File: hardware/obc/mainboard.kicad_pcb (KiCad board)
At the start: 6 copper layers, 95.9 x 90.2 mm, 216 parts, among them J101 Conn_02x20_Odd_Even, J301 USB_C_Receptacle_USB2.0, J302 Conn_High-Rel_4S2P, J303 Conn_01x06, J304 Conn_High-Rel_6P, J305 Conn_01x05, J601 Conn_01x08_Socket, J602 SMA RA Connector, J603 SMA RA Connector, J604 SMA RA Connector, Q201 BSS138DWQ-7, Q202 BSS138DWQ-7, Q203 MBT2222ADW1T1, Q204 MBT2222ADW1T1, Q205 BSS138DWQ-7, Q206 BSS138DWQ-7, Q207 MBT2222ADW1T1, Q208 MBT2222ADW1T1, Q209 MMDT2907, Q401 MBT2222ADW1T1, Q402 MBT2222ADW1T1, Q403 IRLML2803, Q404 IRF7406PbF, Q501 MMBT2222AT, Q502 IRLML2803, Q503 IRLML2803, Q504 IRLML2803, Q505 IRF7406PbF, Q506 IRF7406PbF, Q507 IRF7406PbF, U101 MAX706RESA, U102 ATSAMD51J20A-AU, U103 BMI088, U301 Mem_MT29F4G01ABAFDWB, U302 Mem_MT29F4G01ABAFDWB, U401 TPS7A4501DCQT, U402 LTC4121, U403 TPS54226PWPRPWP14_2P31X2P46-L, U404 ADM1176-1ARMZ-R7, U405 BQ25886RGER, U501 PE014006, U601 RFM98PW, U602 S1216V8, U603 GP2S1+, Y101 32.768kHz

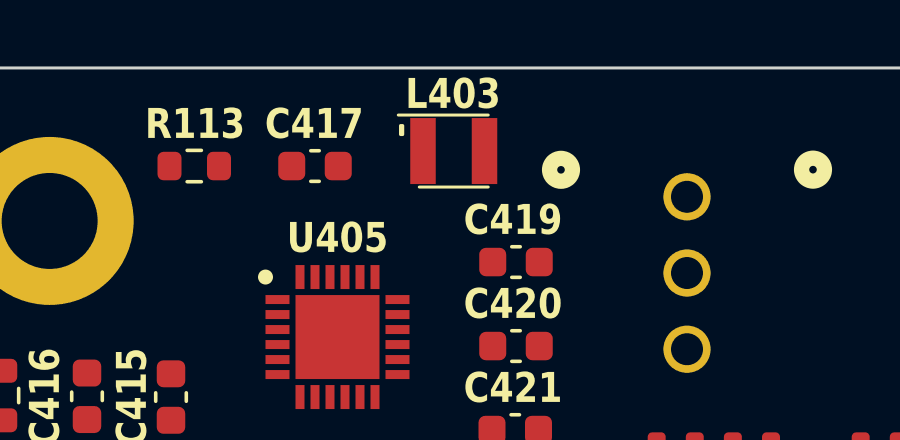
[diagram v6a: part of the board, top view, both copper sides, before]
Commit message: obc: various changes from design review
- change 1008 inductor footprint to one from kicad library
- change 'default class' design rules to match board design rules
- back-annotate from layout to board
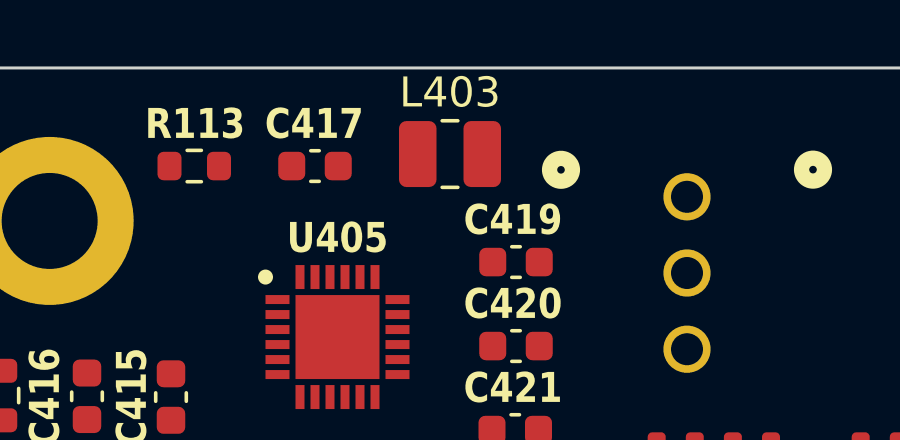
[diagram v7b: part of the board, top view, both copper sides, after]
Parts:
- L403: footprint SSE_Footprints:Murata_1008_2.5x2.0mm -> Inductor_SMD:L_1008_2520Metric
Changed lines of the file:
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@@
 		)
 	)
-	(footprint "SSE_Footprints:Murata_1008_2.5x2.0mm"
+	(footprint "Inductor_SMD:L_1008_2520Metric"
 		(layer "F.Cu")
 		(at 119.3 61.1)
+		(descr "Inductor SMD 1008 (2520 Metric), square (rectangular) end terminal, IPC_7351 nominal, (Body size source: https://ecsxtal.com/store/pdf/ECS-MPI2520-SMD-POWER-INDUCTOR.pdf), generated with kicad-footprint-generator")
+		(tags "inductor")
 		(property "Reference" "L403"
-			(at 0.1 -2 0)
-			(unlocked yes)
+			(at 0 -2.05 0)
 			(layer "F.SilkS")
 			(effects
 				(font
-					(size 1 0.85)
-					(thickness 0.13)
-					(bold yes)
+					(size 1 1)
+					(thickness 0.15)
 				)
 			)
 		)
 		(property "Value" "1uH"
-			(at 0 1.9 0)
-			(unlocked yes)
+			(at 0 2.05 0)
 			(layer "F.Fab")
 			(effects
@@
 			(effects
 				(font
-					(size 1 1)
-					(thickness 0.15)
+					(size 1.27 1.27)
 				)
 			)
@@
 			(effects
 				(font
-					(size 1 1)
-					(thickness 0.15)
+					(size 1.27 1.27)
 				)
 			)
@@
 			(effects
 				(font
-					(size 1 1)
-					(thickness 0.15)
+					(size 1.27 1.27)
 				)
 			)
@@
 			)
 		)
-		(property ki_fp_filters "Choke_* *Coil* Inductor_* L_*")
-		(sheetname "Power")
-		(sheetfile "Power.kicad_sch")
 		(attr smd)
 		(fp_line
-			(start -1.725 -1.3)
-			(end 1.275 -1.3)
-			(stroke
-				(width 0.1)
+			(start -0.261252 -1.11)
+			(end 0.261252 -1.11)
+			(stroke
+				(width 0.12)
 				(type solid)
 			)
@@
 		)
 		(fp_line
-			(start 1.275 1.1)
-			(end -1.025 1.1)
-			(stroke
-				(width 0.1)
+			(start -0.261252 1.11)
+			(end 0.261252 1.11)
+			(stroke
+				(width 0.12)
 				(type solid)
 			)
 			(layer "F.SilkS")
 		)
-		(fp_rect
-			(start -1.65 -0.95)
-			(end -1.575 -0.65)
-			(stroke
-				(width 0.1)
-				(type solid)
-			)
-			(fill solid)
-			(layer "F.SilkS")
-		)
-		(fp_line
-			(start -1.875 -1.4)
-			(end 2.125 -1.4)
-			(stroke
-				(width 0.05)
-				(type solid)
-			)
-			(layer "F.CrtYd")
-		)
-		(fp_line
-			(start -1.875 1.2)
-			(end -1.875 -1.4)
-			(stroke
-				(width 0.05)
-				(type solid)
-			)
-			(layer "F.CrtYd")
-		)
-		(fp_line
-			(start 2.125 -1.4)
-			(end 2.125 1.2)
-			(stroke
-				(width 0.05)
-				(type solid)
-			)
-			(layer "F.CrtYd")
-		)
-		(fp_line
-			(start 2.125 1.2)
-			(end -1.875 1.2)
-			(stroke
-				(width 0.05)
-				(type solid)
-			)
-			(layer "F.CrtYd")
-		)
-		(fp_line
-			(start -1.125 -1.1)
-			(end 1.375 -1.1)
-			(stroke
-				(width 0.1)
-				(type solid)
-			)
-			(layer "F.Fab")
-		)
-		(fp_line
-			(start -1.125 0.9)
-			(end -1.125 -1.1)
-			(stroke
-				(width 0.1)
-				(type solid)
-			)
-			(layer "F.Fab")
-		)
-		(fp_line
-			(start 1.375 -1.1)
-			(end 1.375 0.9)
-			(stroke
-				(width 0.1)
-				(type solid)
-			)
-			(layer "F.Fab")
-		)
-		(fp_line
-			(start 1.375 0.9)
-			(end -1.125 0.9)
+		(fp_line
+			(start -1.95 -1.35)
+			(end 1.95 -1.35)
+			(stroke
+				(width 0.05)
+				(type solid)
+			)
+			(layer "F.CrtYd")
+		)
+		(fp_line
+			(start -1.95 1.35)
+			(end -1.95 -1.35)
+			(stroke
+				(width 0.05)
+				(type solid)
+			)
+			(layer "F.CrtYd")
+		)
+		(fp_line
+			(start 1.95 -1.35)
+			(end 1.95 1.35)
+			(stroke
+				(width 0.05)
+				(type solid)
+			)
+			(layer "F.CrtYd")
+		)
+		(fp_line
+			(start 1.95 1.35)
+			(end -1.95 1.35)
+			(stroke
+				(width 0.05)
+				(type solid)
+			)
+			(layer "F.CrtYd")
+		)
+		(fp_line
+			(start -1.25 -1)
+			(end 1.25 -1)
+			(stroke
+				(width 0.1)
+				(type solid)
+			)
+			(layer "F.Fab")
+		)
+		(fp_line
+			(start -1.25 1)
+			(end -1.25 -1)
+			(stroke
+				(width 0.1)
+				(type solid)
+			)
+			(layer "F.Fab")
+		)
+		(fp_line
+			(start 1.25 -1)
+			(end 1.25 1)
+			(stroke
+				(width 0.1)
+				(type solid)
+			)
+			(layer "F.Fab")
+		)
+		(fp_line
+			(start 1.25 1)
+			(end -1.25 1)
 			(stroke
 				(width 0.1)
@@
 		)
 		(fp_text user "${REFERENCE}"
-			(at -0.1 -0.1 0)
-			(unlocked yes)
-			(layer "F.Fab")
-			(effects
-				(font
-					(size 1 1)
-					(thickness 0.15)
-				)
-			)
-		)
-		(pad "1" smd rect
-			(at -0.9 -0.1)
-			(size 0.85 2.2)
+			(at 0 0 0)
+			(layer "F.Fab")
+			(effects
+				(font
+					(size 0.62 0.62)
+					(thickness 0.09)
+				)
+			)
+		)
+		(pad "1" smd roundrect
+			(at -1.075 0)
+			(size 1.25 2.2)
 			(layers "F.Cu" "F.Paste" "F.Mask")
+			(roundrect_rratio 0.2)
 			(net 30 "Net-(U405-PMID_1)")
 			(pinfunction "1")
 			(pintype "passive")
 		)
-		(pad "2" smd rect
-			(at 1.15 -0.1)
-			(size 0.85 2.2)
+		(pad "2" smd roundrect
+			(at 1.075 0)
+			(size 1.25 2.2)
 			(layers "F.Cu" "F.Paste" "F.Mask")
+			(roundrect_rratio 0.2)
 			(net 31 "Net-(U405-SW_1)")
 			(pinfunction "2")
 			(pintype "passive")
 		)
+		(model "${KICAD8_3DMODEL_DIR}/Inductor_SMD.3dshapes/L_1008_2520Metric.wrl"
+			(offset
+				(xyz 0 0 0)
+			)
+			(scale
+				(xyz 1 1 1)
+			)
+			(rotate
+				(xyz 0 0 0)
+			)
+		)
 	)

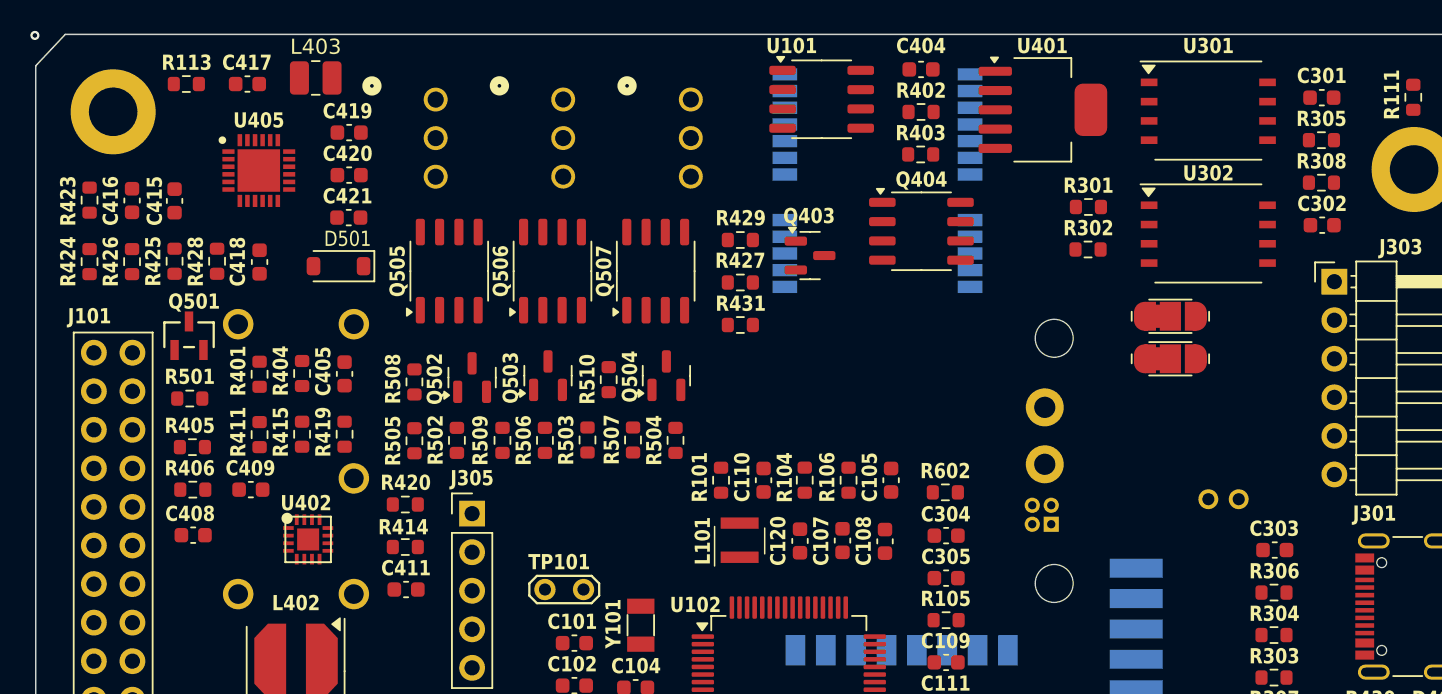
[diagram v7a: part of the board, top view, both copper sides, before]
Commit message: obc: entered footprint and routed traces in a test subsection
Made harwin battery connector vertical and routed traces around U405 component.
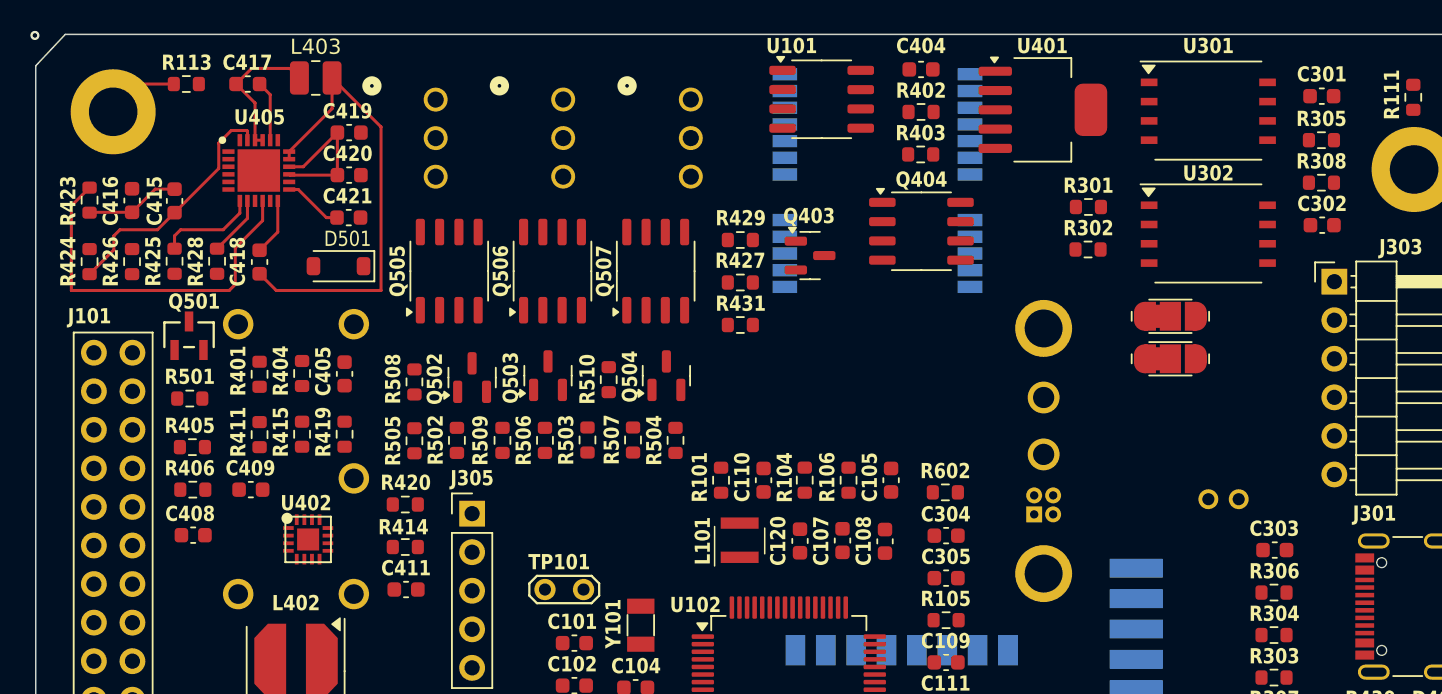
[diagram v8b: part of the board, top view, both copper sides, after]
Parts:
- J302: value Conn_High-Rel_4S2P -> Conn_High-Rel_4S2P_Vertical; footprint SSE_Footprints:Harwin_G125-MH104M3-02AD000P_4S2P_P1.25mm_Horizontal -> SSE_Footprints:Harwin_G125-FV104F3-02AB000P_P1.25mm_Vertical
- moved J302 0.93 mm to (168.0, 85.5)
- moved C301 0.10 mm to (185.6, 62.3)
- turned C417 to 180 degrees
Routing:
- net Net-(U405-SW_1): track 0.00 -> 30.3 mm
- net Net-(U405-ICHGSET): track 0.00 -> 24.5 mm
- net VBUS_IN: track 0.00 -> 16.5 mm
- net GNDREF: track 0.00 -> 10.2 mm
- net SYS_1&2: track 0.00 -> 10.1 mm
- net Net-(U405-PMID_1): track 0.00 -> 9.65 mm
- net THM: track 0.00 -> 6.57 mm
- net Net-(H104-Pad1): track 0.00 -> 4.99 mm
- net Net-(U405-ILIM): track 0.00 -> 3.98 mm
- net BAT_1&2: track 0.00 -> 3.92 mm
- net Net-(U405-BTST): track 0.00 -> 3.75 mm
